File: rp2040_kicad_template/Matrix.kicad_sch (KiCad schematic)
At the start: 20 parts

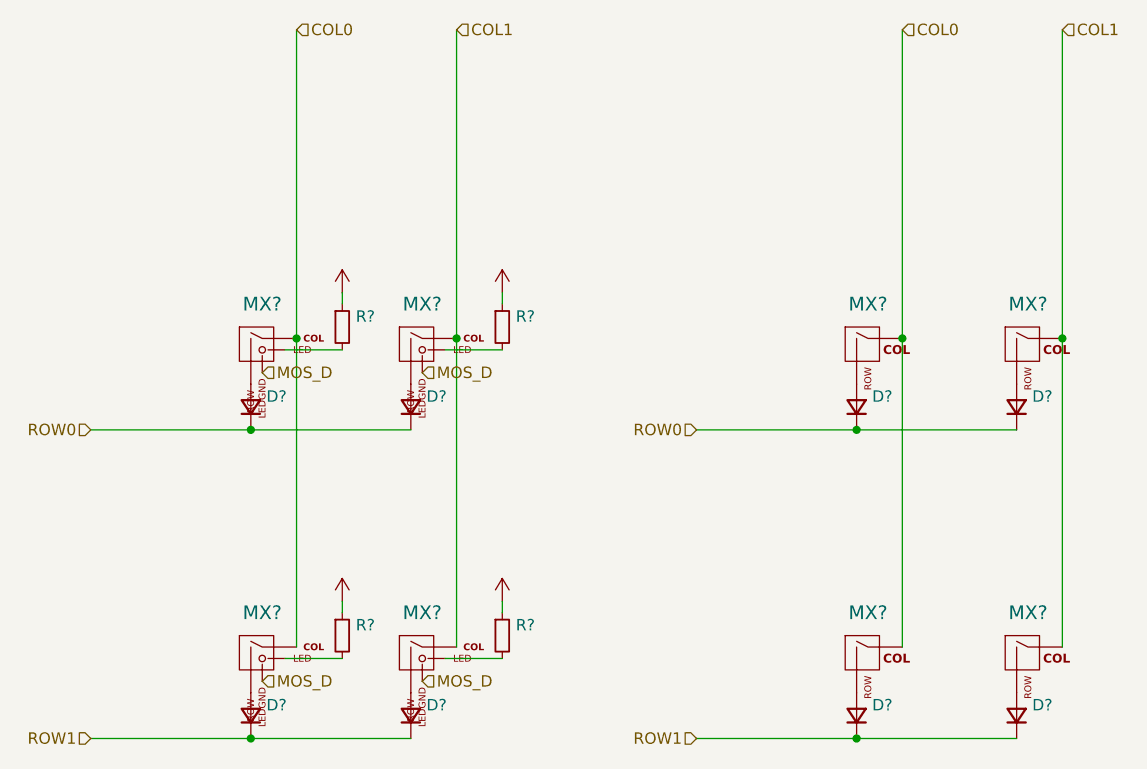
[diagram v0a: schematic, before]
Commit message: Migrate libraries to KiCAD 6
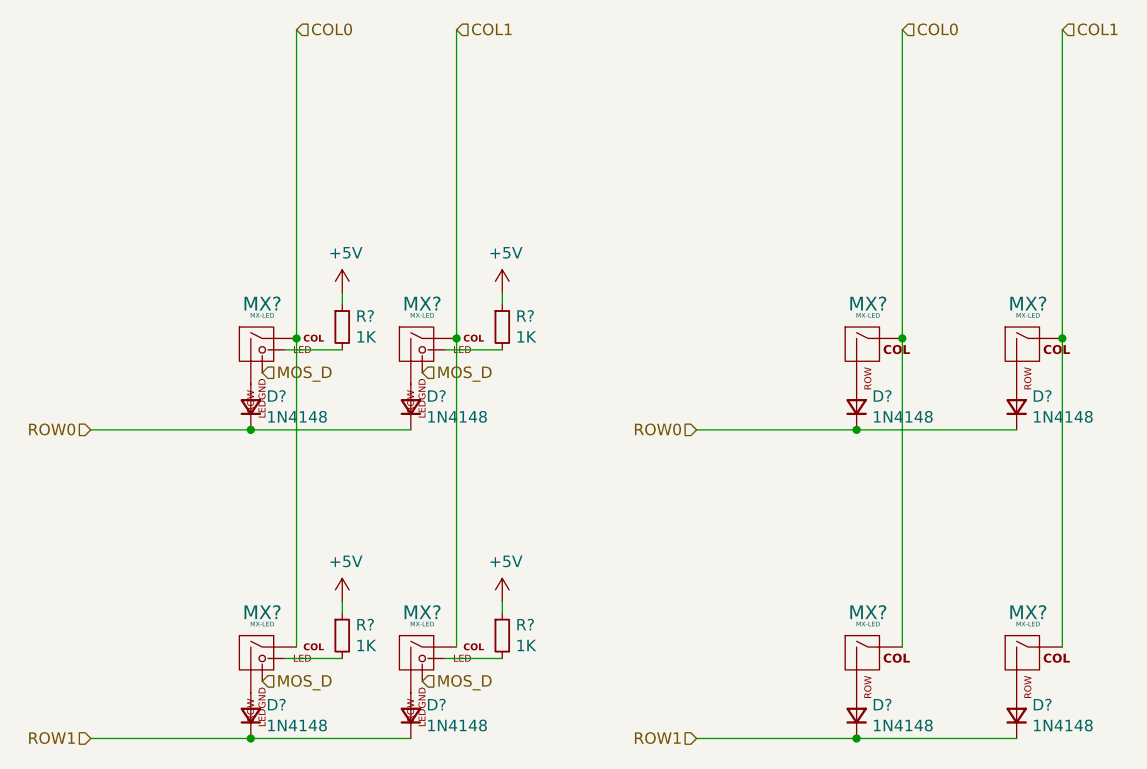
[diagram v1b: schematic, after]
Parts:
- D? (x8): value (none) -> 1N4148; footprint (none) -> random-keyboard-parts:D_SOD-123-Pretty
- MX? (x4): value (none) -> MX-LED; footprint (none) -> MX_Only:MXOnly-1U
- MX? (x4): value (none) -> MX-LED; footprint (none) -> MX_Only:MXOnly-1U-NoLED
- R? (x4): value (none) -> 1K; footprint (none) -> Resistor_SMD:R_0805_2012Metric

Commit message: Add level shifter to RP2040 template
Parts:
- R? (x4): footprint Resistor_SMD:R_0805_2012Metric -> (none)
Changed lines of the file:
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@@
       (effects (font (size 1.27 1.27)) (justify left))
     )
-    (property "Footprint" "Resistor_SMD:R_0805_2012Metric" (id 2) (at 52.07 48.26 0)
+    (property "Footprint" "" (id 2) (at 52.07 48.26 0)
       (effects (font (size 1.27 1.27)) hide)
     )
@@
       (effects (font (size 1.27 1.27)) (justify left))
     )
-    (property "Footprint" "Resistor_SMD:R_0805_2012Metric" (id 2) (at 69.85 48.26 0)
+    (property "Footprint" "" (id 2) (at 69.85 48.26 0)
       (effects (font (size 1.27 1.27)) hide)
     )
@@
       (effects (font (size 1.27 1.27)) (justify left))
     )
-    (property "Footprint" "Resistor_SMD:R_0805_2012Metric" (id 2) (at 52.07 82.55 0)
+    (property "Footprint" "" (id 2) (at 52.07 82.55 0)
       (effects (font (size 1.27 1.27)) hide)
     )
@@
       (effects (font (size 1.27 1.27)) (justify left))
     )
-    (property "Footprint" "Resistor_SMD:R_0805_2012Metric" (id 2) (at 69.85 82.55 0)
+    (property "Footprint" "" (id 2) (at 69.85 82.55 0)
       (effects (font (size 1.27 1.27)) hide)
     )

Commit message: Update RP2040 to use 27 ohm resistors
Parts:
- R? (x4): footprint (none) -> Resistor_SMD:R_0402_1005Metric
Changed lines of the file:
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@@
       (effects (font (size 1.27 1.27)) (justify left))
     )
-    (property "Footprint" "" (id 2) (at 52.07 48.26 0)
+    (property "Footprint" "Resistor_SMD:R_0402_1005Metric" (id 2) (at 52.07 48.26 0)
       (effects (font (size 1.27 1.27)) hide)
     )
@@
       (effects (font (size 1.27 1.27)) (justify left))
     )
-    (property "Footprint" "" (id 2) (at 69.85 48.26 0)
+    (property "Footprint" "Resistor_SMD:R_0402_1005Metric" (id 2) (at 69.85 48.26 0)
       (effects (font (size 1.27 1.27)) hide)
     )
@@
       (effects (font (size 1.27 1.27)) (justify left))
     )
-    (property "Footprint" "" (id 2) (at 52.07 82.55 0)
+    (property "Footprint" "Resistor_SMD:R_0402_1005Metric" (id 2) (at 52.07 82.55 0)
       (effects (font (size 1.27 1.27)) hide)
     )
@@
       (effects (font (size 1.27 1.27)) (justify left))
     )
-    (property "Footprint" "" (id 2) (at 69.85 82.55 0)
+    (property "Footprint" "Resistor_SMD:R_0402_1005Metric" (id 2) (at 69.85 82.55 0)
       (effects (font (size 1.27 1.27)) hide)
     )
